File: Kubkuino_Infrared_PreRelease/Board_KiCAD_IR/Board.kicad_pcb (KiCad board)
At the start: 2 copper layers, 31 parts, among them J1 Piezo, J2 Conn_01x03, J3 I2C, J4 Conn_01x03, J6 AC/DC In (12V), J7 Bluetooth, J8 Button, Q1 S8050, U1 ATMEGA328P-AU, U2 LM7805_TO220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

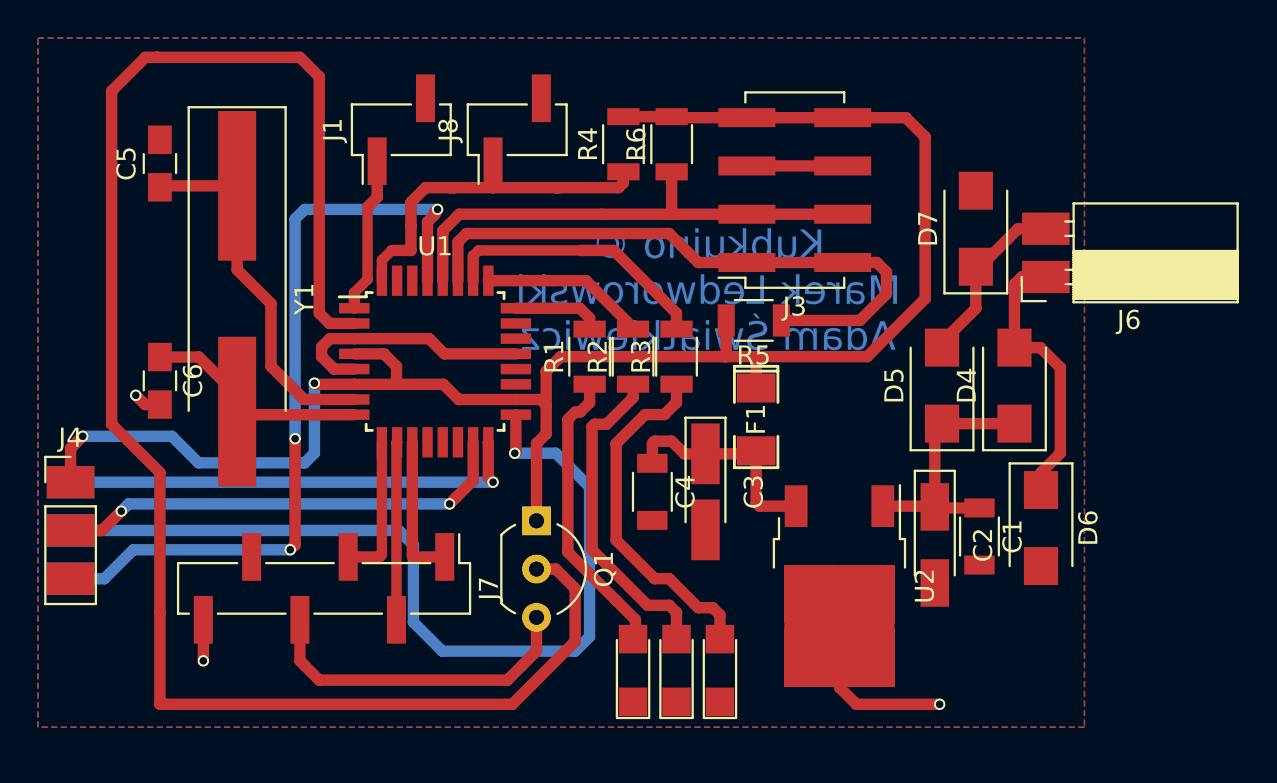
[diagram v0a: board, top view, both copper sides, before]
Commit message: Updates
Finished new board
Changed SSD1306 to 128x64
Major RAM optimization
Main routine optimizations
Set up display layout
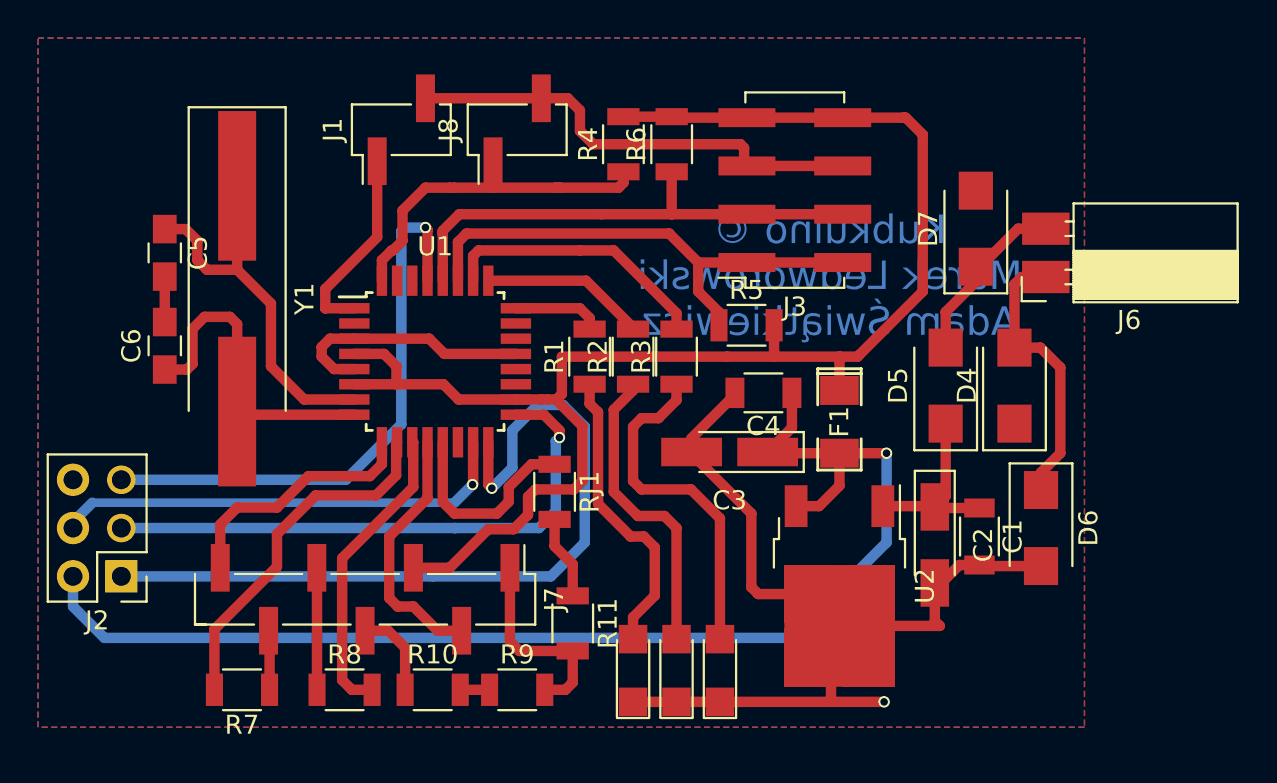
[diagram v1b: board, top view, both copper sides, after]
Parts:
- removed J4: Conn_01x03, Socket_Strips:Socket_Strip_Straight_1x03_Pitch2.54mm
- removed Q1: S8050, TO_SOT_Packages_THT:TO-92_Inline_Wide
- added R10: 4k7, Resistors_SMD:R_1206, F.Cu at (135.5, 111.0)
- added R11: 4k7, Resistors_SMD:R_1206, F.Cu at (142.9, 107.5)
- added R7: 4k7, Resistors_SMD:R_1206, F.Cu at (125.5, 111.0)
- added R8: 4k7, Resistors_SMD:R_1206, F.Cu at (130.9, 111.0)
- added R9: 4k7, Resistors_SMD:R_1206, F.Cu at (140.0, 111.0)
- added RJ1: 0, Resistors_SMD:R_1206, F.Cu at (141.9, 100.6)
- J2: value Conn_01x03 -> Conn_02x03_Odd_Even; footprint Socket_Strips:Socket_Strip_Straight_1x03_Pitch2.54mm -> Pin_Headers:Pin_Header_Straight_2x03_Pitch2.54mm; moved to F.Cu
- J7: footprint Pin_Headers:Pin_Header_Straight_1x06_Pitch2.54mm_SMD_Pin1Left -> Pin_Headers:Pin_Header_Straight_1x07_Pitch2.54mm_SMD_Pin1Left
- moved C4 7.83 mm to (152.9, 95.4), turned to 180 degrees
- moved J2 5.63 mm to (119.1, 105.0)
- moved C5 4.71 mm to (121.4, 88.0), turned to 270 degrees
- moved F1 4.38 mm to (156.9, 96.9)
- moved C3 2.45 mm to (151.1, 98.5), turned to 180 degrees
- moved J7 2.23 mm to (132.0, 106.2)
- moved C6 1.86 mm to (121.4, 92.9), turned to 90 degrees
- moved R5 0.46 mm to (152.0, 91.8), turned to 0 degrees
- moved D5 0.19 mm to (162.5, 95.0)
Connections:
- J2 pad 2: Net-(J2-Pad2) -> Net-(C3-Pad1)
- J2 pad 3: Reset -> Net-(J2-Pad3)
- J7 pad 1: Bkey -> Net-(J7-Pad1)
- J7 pad 2: Brx -> BTen
- J7 pad 3: Btx -> 5V
- J7 pad 4: Net-(J7-Pad4) -> GND
- J7 pad 6: GND -> Net-(J7-Pad6)
- U1 pad 11: Bkey -> Btx
- U1 pad 12: 1W -> BTen
- U1 pad 13: Net-(U1-Pad13) -> BTkey
- U1 pad 14: Net-(U1-Pad14) -> (no net)
- U1 pad 15: Net-(J4-Pad2) -> Net-(J2-Pad4)
- U1 pad 17: Net-(J2-Pad2) -> Net-(J2-Pad3)
- U1 pad 2: BT -> Net-(U1-Pad2)
- U1 pad 9: Btx -> BtConn
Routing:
- net BT: track 88.5 -> 0.00 mm
- net GND: track 31.2 -> 91.6 mm, vias 3 -> 1
- net Net-(C3-Pad1): track 11.9 -> 66.2 mm, vias 0 -> 1
- net Net-(J2-Pad2): track 47.2 -> 0.00 mm, vias 1 -> 0
- net Net-(J2-Pad3): track 0.00 -> 30.3 mm, vias 0 -> 1
- net Net-(J2-Pad4): track 0.00 -> 24.4 mm, vias 0 -> 1
- net Net-(J4-Pad2): track 24.3 -> 0.00 mm, vias 2 -> 0
- net Net-(J2-Pad1): track 24.4 -> 42.0 mm
- net Net-(J7-Pad4): track 17.4 -> 0.00 mm
- net BTen: track 0.00 -> 13.6 mm
- net BtConn: track 0.00 -> 13.3 mm
- net 5V: track 94.0 -> 81.9 mm, vias 2 -> 0
- net Reset: track 41.4 -> 30.3 mm, vias 3 -> 1
- net BTkey: track 0.00 -> 10.8 mm
- net Net-(J7-Pad1): track 0.00 -> 10.7 mm
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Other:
- net class Default: trace_width 0.6 -> 0.55
